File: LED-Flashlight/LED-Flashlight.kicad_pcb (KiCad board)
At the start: 2 copper layers, 24.5 x 17 mm, 10 parts, among them IC1 TLV61220, SW1 SW_SKRPABE010

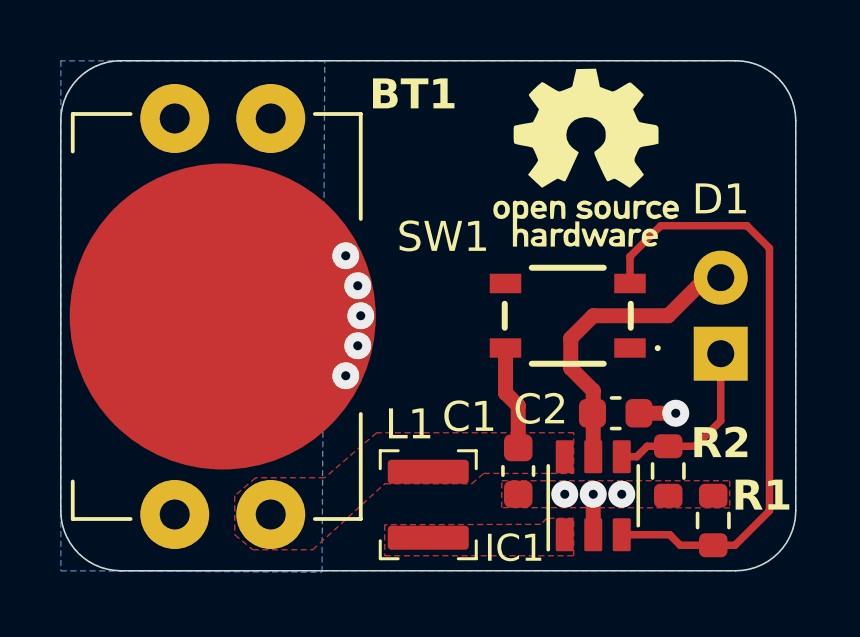
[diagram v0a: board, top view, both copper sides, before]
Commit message: added milling files, lib changes, added footprint tables, changed to kicad 10 format
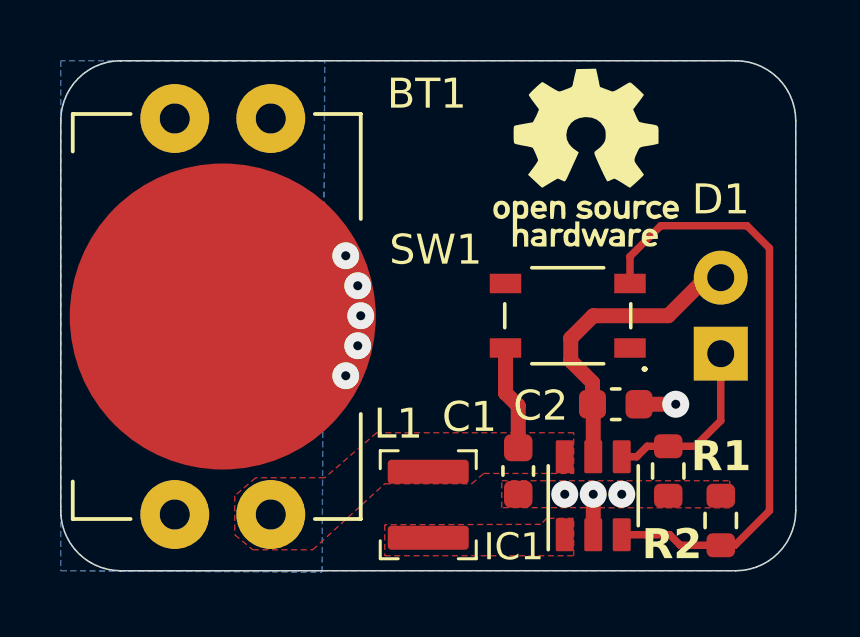
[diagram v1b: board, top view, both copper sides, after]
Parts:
- BT1: footprint Keyring-flashlight:BAT_BAT-HLD-012-THM-TR -> Keychain-flashlight:BAT_BAT-HLD-012-THM-TR
- C1, C2: footprint Keyring-flashlight:C_0603_1608Metric -> Keychain-flashlight:C_0603_1608Metric
- D1: footprint Keyring-flashlight:LED_D5.0mm_Horizontal_O1.27mm_Z3.0mm_Clear -> Keychain-flashlight:LED_D5.0mm_Horizontal_O1.27mm_Z3.0mm_Clear
- IC1: footprint Keyring-flashlight:SOT23-6P095_300X290L70 -> Keychain-flashlight:SOT23-6P095_300X290L70
- L1: footprint Keyring-flashlight:Murata_2.7x3mm_LQH3NP-Series -> Keychain-flashlight:Murata_2.7x3mm_LQH3NP-Series
- R1, R2: footprint Keyring-flashlight:R_0603_1608Metric -> Keychain-flashlight:R_0603_1608Metric
- REF**: value LOGO -> LOGO OSH 6x6 mm; footprint Keyring-flashlight:LOGO OSH 6x6 mm -> Keychain-flashlight:LOGO OSH 6x6 mm
- SW1: footprint Keyring-flashlight:Alps_SKRPABE010_4.2x3.2 -> Keychain-flashlight:Alps_SKRPABE010_4.2x3.2
- moved C2 0.30 mm to (158.5, 114.5)
- moved R1 0.25 mm to (162.0, 118.3)
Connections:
- SW1 pad 1: +VBAT -> unconnected-(SW1-Pad1)
- SW1 pad 4: /SW_EN -> unconnected-(SW1-A-Pad4)
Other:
- board text added: "${TITLE} ${REVISION}"
- board text added: "Assembly Drawing"
